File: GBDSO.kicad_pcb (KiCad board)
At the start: 2 copper layers, 85 x 61 mm, 80 parts, among them J1 MJ-3523-SMT-TR, J2 MJ-3523-SMT-TR, J3 EdgeConnector, J4 GameBoy Cartridge Connector, J5 Conn_01x02, J6 Conn_01x02, P1 100k, P2 100k, SW1 SW_SPDT, SW2 SW_SPDT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

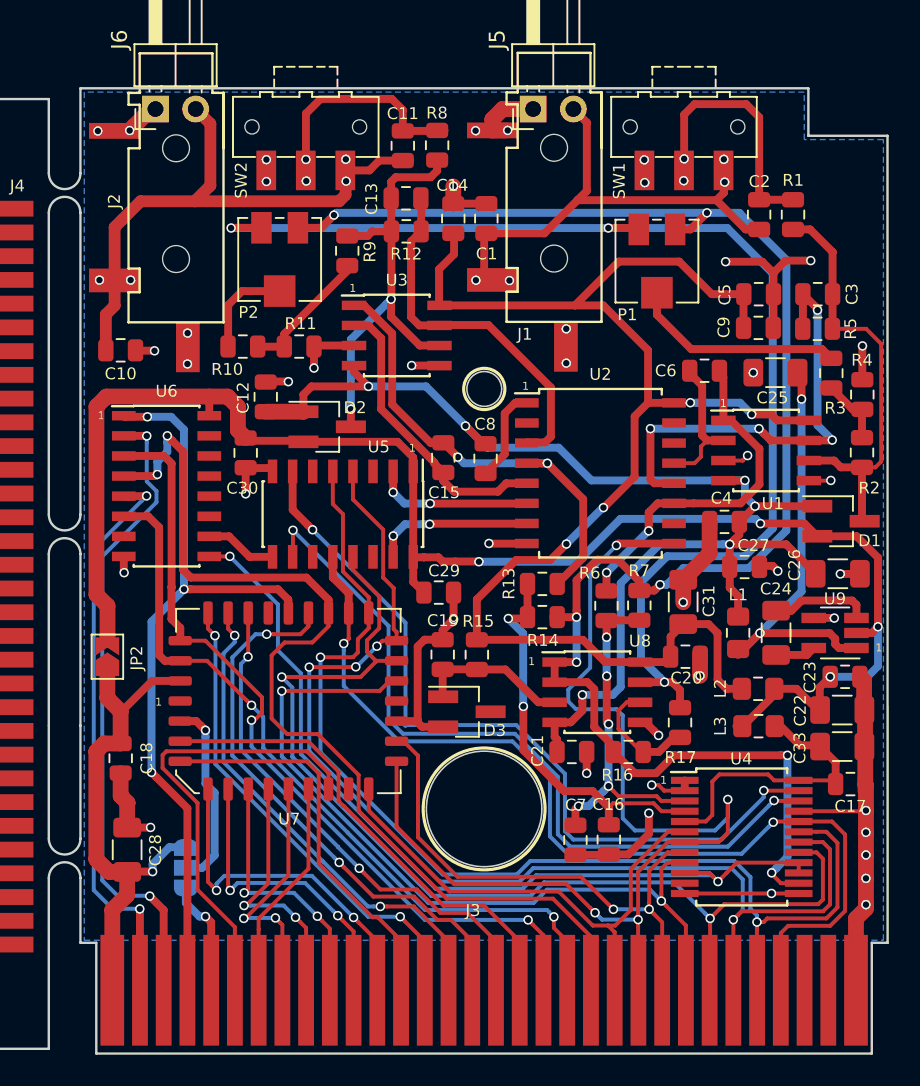
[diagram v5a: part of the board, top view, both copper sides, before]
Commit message: Changed TL062 to TL072, #14. Added silkscreen for channels, #8. Updated PCB images, #11
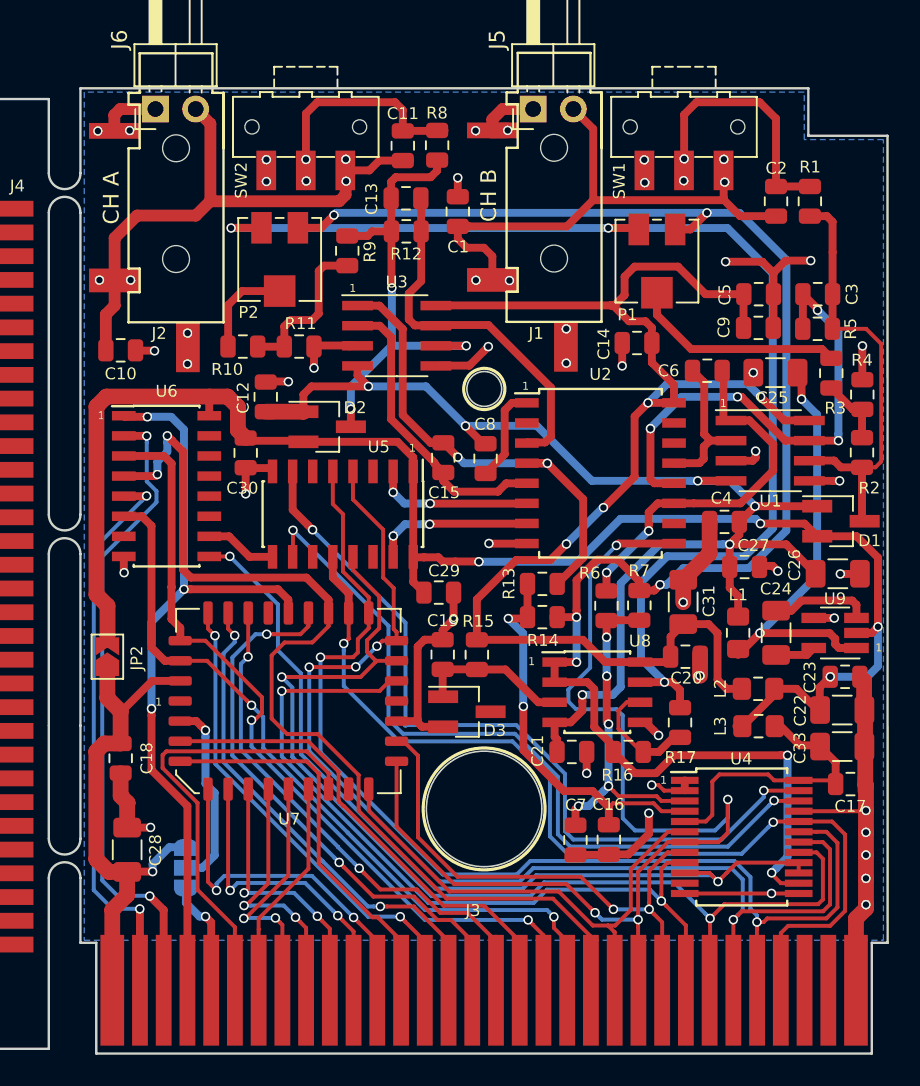
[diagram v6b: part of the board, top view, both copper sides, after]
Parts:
- U1, U3: value TL062 -> TL072
- moved C14 14.0 mm to (173.6, 85.7), turned to 180 degrees
- moved C1 1.86 mm to (162.3, 77.4)
- moved C2 1.36 mm to (182.4, 76.8)
- moved R1 1.36 mm to (184.5, 76.8)
- moved U1 0.26 mm to (182.0, 92.5)
- moved C6 0.18 mm to (178.0, 87.5)
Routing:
- net Net-(C1-Pad1): track 32.3 -> 37.2 mm
- net GND: track 185.4 -> 189.3 mm, vias 37 -> 38
- net +5VA: track 91.0 -> 88.5 mm
- net Net-(C3-Pad2): track 28.8 -> 31.1 mm
- net Net-(C13-Pad1): track 28.3 -> 30.0 mm, vias 2 -> 3
- net Net-(R10-Pad2): track 8.38 -> 10.0 mm
- net Net-(C6-Pad2): track 22.4 -> 23.7 mm
- net Net-(C25-Pad1): track 26.3 -> 27.1 mm
- net Net-(C10-Pad1): track 38.4 -> 37.6 mm
- net Net-(C15-Pad1): track 30.3 -> 30.9 mm
- net Net-(C6-Pad1): track 8.99 -> 9.52 mm
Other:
- board text added: "CH A"
- board text added: "CH B"

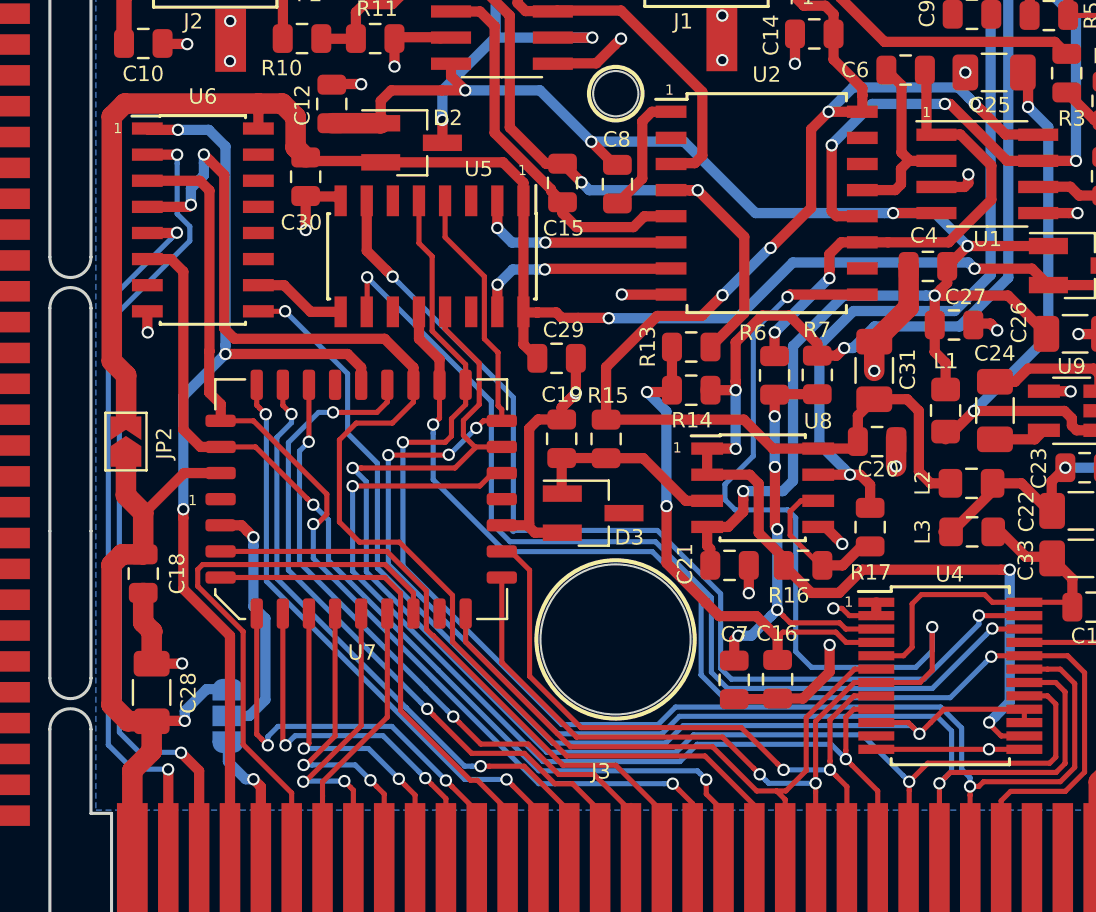
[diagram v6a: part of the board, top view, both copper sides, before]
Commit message: fix #16
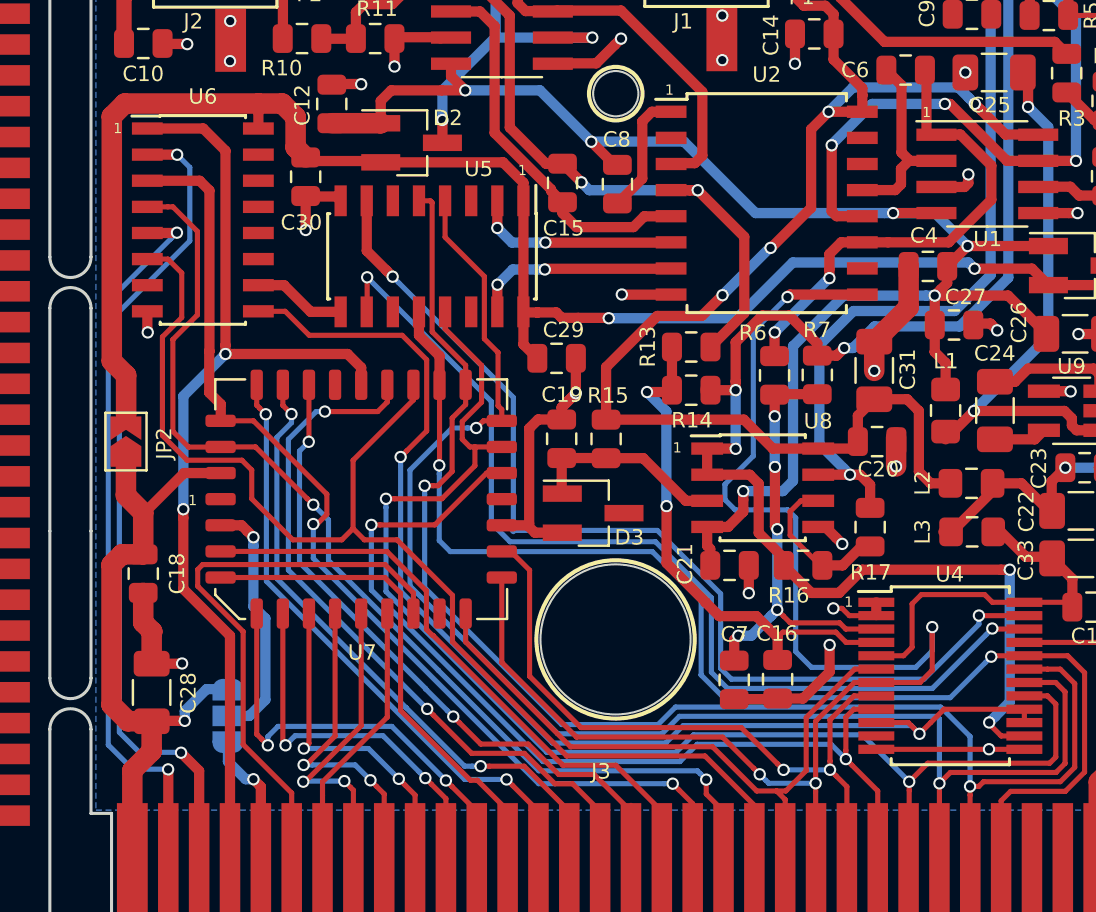
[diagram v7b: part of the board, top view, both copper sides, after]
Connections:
- U6 pad 4: /GBDSO Cartridge/A15 -> /GBDSO Cartridge/A14
- U6 pad 6: /GBDSO Cartridge/A14 -> /GBDSO Cartridge/A15
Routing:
- net /GBDSO Cartridge/A14: track 48.2 -> 52.2 mm
- net Net-(U4-Pad10): track 54.6 -> 58.3 mm
- net /GBDSO Cartridge/A15: track 64.3 -> 60.6 mm, vias 2 -> 0
- net /GBDSO Cartridge/D5: track 74.1 -> 71.7 mm, vias 4 -> 2
- net /GBDSO Cartridge/D4: track 68.5 -> 66.1 mm
- net /GBDSO Cartridge/D3: track 49.9 -> 47.6 mm
- net /GBDSO Cartridge/D6: track 71.8 -> 70.4 mm
- net /GBDSO Cartridge/D7: track 61.1 -> 62.4 mm
- net +5V: track 136.8 -> 136.2 mm
- net /GBDSO Cartridge/~RD: track 49.0 -> 48.9 mm, vias 3 -> 2

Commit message: issue #16, #17 and #18 are fixed in the schematic but not yet in the PCB
reopened issue #16 and #17 as they were not yet fixed in the PCB
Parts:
- removed REF** (x2): OSHW-Symbol_6.7x6mm_SilkScreen, Symbol:OSHW-Symbol_6.7x6mm_SilkScreen
- removed REF**: KiCad-Logo_6mm_SilkScreen, Symbol:KiCad-Logo_6mm_SilkScreen
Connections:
- C8 pad 1: Net-(C8-Pad1) -> -5V
- C8 pad 2: -5V -> GND
- D1 pad 2: +5V -> +5VA
- D2 pad 2: +5V -> +5VA
- U2 pad 1: Net-(C8-Pad1) -> -5V
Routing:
- net -5V: track 80.5 -> 86.6 mm
- net Net-(C8-Pad1): track 6.09 -> 0.00 mm
